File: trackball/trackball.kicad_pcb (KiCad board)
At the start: 2 copper layers, 15 x 27.4 mm, 7 parts, among them P8 CONN_7, U1 TLE4964-5M, U2 TLE4964-5M, U3 TLE4964-5M, U4 TLE4964-5M

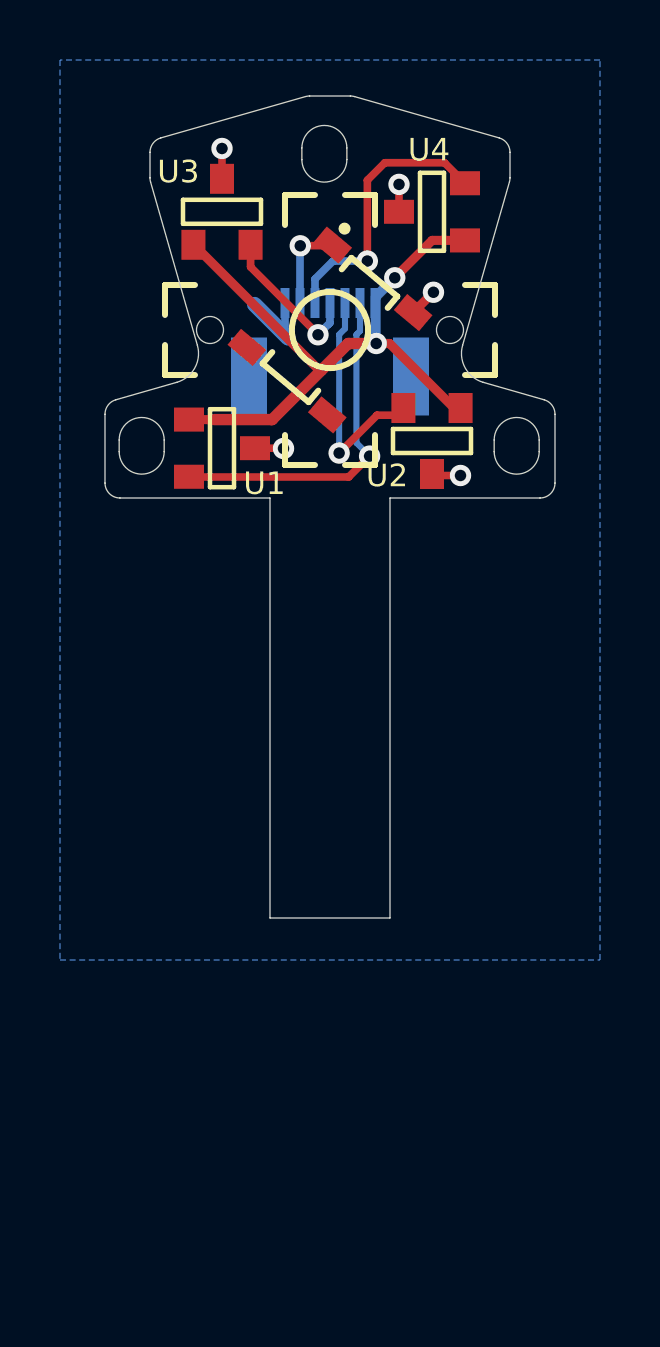
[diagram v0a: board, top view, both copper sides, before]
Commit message: Add most FPC tracks.
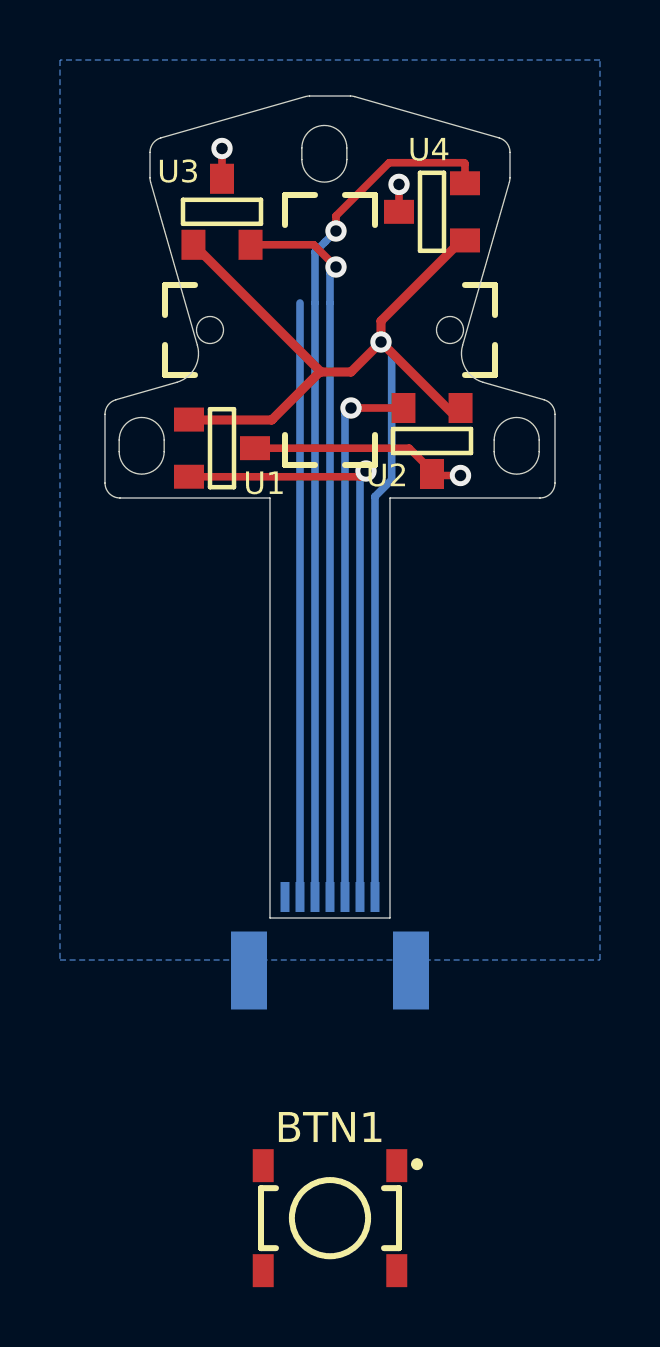
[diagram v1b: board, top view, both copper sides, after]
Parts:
- moved BTN1 29.6 mm to (200.0, 179.6), turned to 0 degrees
- moved P8 19.8 mm to (200.0, 172.9)
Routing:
- net /TB_RIGHT: track 9.58 -> 29.4 mm
- net /TB_UP: track 5.15 -> 24.5 mm
- net +3V3: track 22.5 -> 40.2 mm, vias 2 -> 1
- net /TB_BTN: track 4.14 -> 20.2 mm, vias 1 -> 0
- net /TB_DOWN: track 7.85 -> 18.5 mm
- net /TB_LEFT: track 11.5 -> 20.6 mm
- net GND: track 7.25 -> 9.03 mm, vias 5 -> 3

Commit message: Fix switch position and orientation.
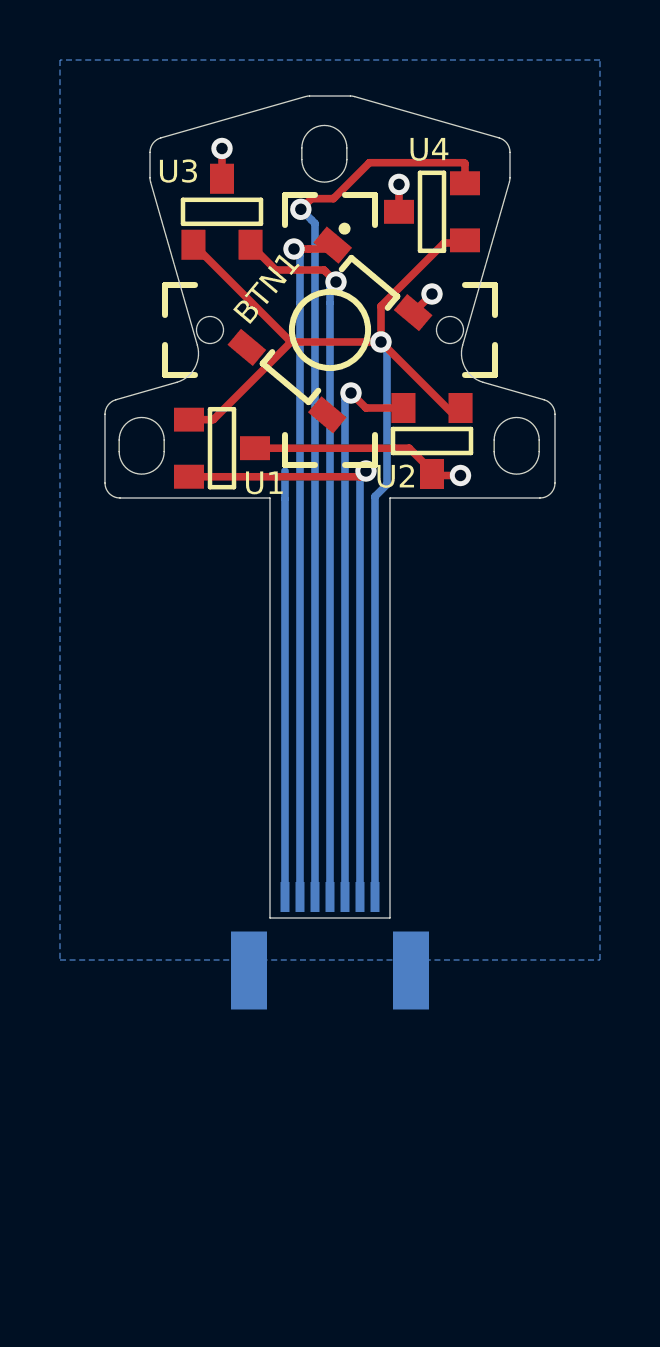
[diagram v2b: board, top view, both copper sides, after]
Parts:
- moved BTN1 29.6 mm to (200.0, 150.0), turned to 50 degrees
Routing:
- net GND: track 9.03 -> 24.1 mm, vias 3 -> 4
- net /TB_BTN: track 20.2 -> 23.1 mm, vias 0 -> 1
- net /TB_RIGHT: track 29.4 -> 30.6 mm
- net +3V3: track 40.2 -> 39.5 mm
- net /TB_DOWN: track 18.5 -> 19.2 mm
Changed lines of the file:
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@@
     (thickness 1.6)
     (drawings 46)
-    (tracks 57)
+    (tracks 68)
     (zones 0)
     (modules 7)
@@
     (tags SOT23)
     (attr smd)
-    (fp_text reference U2 (at 1.5 -1.16) (layer F.SilkS)
+    (fp_text reference U2 (at 1.2 -1.2) (layer F.SilkS)
       (effects (font (size 0.75 0.75) (thickness 0.15)))
     )
@@
   )
   (module UGL:TL3315NF250Q (layer F.Cu)
-    (at 200.000001 179.605001)
-    (fp_text reference BTN1 (at 0 -3) (layer F.SilkS)
-      (effects (font (size 1 1) (thickness 0.15)))
-    )
-    (fp_text value BTN (at 0 3.1) (layer F.Fab)
+    (at 200 150 50)
+    (fp_text reference BTN1 (at -0.277392 -2.508596 50) (layer F.SilkS)
+      (effects (font (size 0.75 0.75) (thickness 0.15)))
+    )
+    (fp_text value BTN (at 0 3.1 50) (layer F.Fab)
       (effects (font (size 1 1) (thickness 0.15)))
     )
@@
     (fp_line (start 2.3 1) (end 2.3 -1) (layer F.SilkS) (width 0.2))
     (fp_circle (center 2.9 -1.8) (end 3 -1.8) (layer F.SilkS) (width 0.2))
-    (pad 2 smd rect (at 2.225 1.75) (size 0.7 1.1) (layers F.Cu F.Paste F.Mask)
+    (pad 2 smd rect (at 2.225 1.75 50) (size 0.7 1.1) (layers F.Cu F.Paste F.Mask)
       (net 1 GND))
-    (pad 3 smd rect (at -2.225 1.75 180) (size 0.7 1.1) (layers F.Cu F.Paste F.Mask))
-    (pad 1 smd rect (at 2.225 -1.75) (size 0.7 1.1) (layers F.Cu F.Paste F.Mask)
+    (pad 3 smd rect (at -2.225 1.75 230) (size 0.7 1.1) (layers F.Cu F.Paste F.Mask))
+    (pad 1 smd rect (at 2.225 -1.75 50) (size 0.7 1.1) (layers F.Cu F.Paste F.Mask)
       (net 2 /TB_BTN))
-    (pad 4 smd rect (at -2.225 -1.75 180) (size 0.7 1.1) (layers F.Cu F.Paste F.Mask))
+    (pad 4 smd rect (at -2.225 -1.75 230) (size 0.7 1.1) (layers F.Cu F.Paste F.Mask))
   )
   (gr_line (start 202 155.6) (end 207 155.6) (angle 90) (layer Edge.Cuts) (width 0.01))
@@
   (segment (start 197.49982 153.94) (end 202.64 153.94) (width 0.254) (layer F.Cu) (net 1))
   (segment (start 202.64 153.94) (end 203.3 154.6) (width 0.254) (layer F.Cu) (net 1))
+  (via (at 203.4 148.8) (size 0.7112) (drill 0.381) (layers F.Cu B.Cu) (net 1))
+  (segment (start 202.77078 149.420429) (end 202.779571 149.420429) (width 0.254) (layer F.Cu) (net 1))
+  (segment (start 202.779571 149.420429) (end 203.4 148.8) (width 0.254) (layer F.Cu) (net 1))
+  (segment (start 198.5 168.9) (end 198.5 155.625942) (width 0.254) (layer B.Cu) (net 1))
+  (segment (start 198.5 155.625942) (end 198.5 154.7) (width 0.254) (layer B.Cu) (net 1))
   (segment (start 199 149.1) (end 199 169.26479) (width 0.254) (layer B.Cu) (net 2))
+  (via (at 198.8 147.3) (size 0.7112) (drill 0.381) (layers F.Cu B.Cu) (net 2))
+  (segment (start 199 149.1) (end 199 147.5) (width 0.254) (layer B.Cu) (net 2))
+  (segment (start 199 147.5) (end 198.8 147.3) (width 0.254) (layer B.Cu) (net 2))
+  (segment (start 198.8 147.3) (end 199.302894 147.3) (width 0.254) (layer F.Cu) (net 2))
+  (segment (start 199.302894 147.3) (end 199.9 147.3) (width 0.254) (layer F.Cu) (net 2))
   (segment (start 195.30018 154.8925) (end 195.30768 154.9) (width 0.254) (layer F.Cu) (net 3))
   (segment (start 201.0075 154.8925) (end 201.2 154.7) (width 0.254) (layer F.Cu) (net 3))
@@
   (segment (start 201.602894 150.5) (end 201.6 150.5) (width 0.3048) (layer F.Cu) (net 4))
   (via (at 201.7 150.4) (size 0.7112) (drill 0.381) (layers F.Cu B.Cu) (net 4))
-  (segment (start 201.7 150.4) (end 201.7 149.7) (width 0.3048) (layer F.Cu) (net 4))
-  (segment (start 201.7 149.7) (end 204.2 147.2) (width 0.3048) (layer F.Cu) (net 4))
-  (segment (start 198.071162 152.9875) (end 198.058662 153) (width 0.3048) (layer F.Cu) (net 4))
-  (segment (start 198.058662 153) (end 195.5 153) (width 0.3048) (layer F.Cu) (net 4))
-  (segment (start 198.071162 152.9875) (end 199.658662 151.4) (width 0.3048) (layer F.Cu) (net 4))
-  (segment (start 201.7 150.4) (end 200.7 151.4) (width 0.3048) (layer F.Cu) (net 4))
-  (segment (start 200.7 151.4) (end 199.7 151.4) (width 0.3048) (layer F.Cu) (net 4))
-  (segment (start 199.7 151.4) (end 195.6 147.3) (width 0.3048) (layer F.Cu) (net 4))
   (segment (start 201.75 150.45) (end 201.7 150.45) (width 0.3048) (layer F.Cu) (net 4))
   (segment (start 201.7 150.45) (end 201.7 150.4) (width 0.3048) (layer F.Cu) (net 4))
   (segment (start 204.3525 152.84018) (end 204.14018 152.84018) (width 0.3048) (layer F.Cu) (net 4))
-  (segment (start 204.14018 152.84018) (end 201.75 150.45) (width 0.3048) (layer F.Cu) (net 4))
-  (segment (start 202.055599 154.993888) (end 201.5 155.549487) (width 0.254) (layer B.Cu) (net 4))
-  (segment (start 202.055599 150.755599) (end 202.055599 154.993888) (width 0.254) (layer B.Cu) (net 4))
-  (segment (start 201.7 150.4) (end 202.055599 150.755599) (width 0.254) (layer B.Cu) (net 4))
+  (segment (start 195.30018 152.9875) (end 196.1125 152.9875) (width 0.254) (layer F.Cu) (net 4))
+  (segment (start 196.1125 152.9875) (end 198.7 150.4) (width 0.254) (layer F.Cu) (net 4))
+  (segment (start 201.7 150.4) (end 198.7 150.4) (width 0.254) (layer F.Cu) (net 4))
+  (segment (start 198.7 150.4) (end 195.6 147.3) (width 0.254) (layer F.Cu) (net 4))
+  (segment (start 201.7 149.206222) (end 203.806222 147.1) (width 0.254) (layer F.Cu) (net 4))
+  (segment (start 201.7 150.4) (end 201.7 149.206222) (width 0.254) (layer F.Cu) (net 4))
+  (segment (start 203.806222 147.1) (end 204.3 147.1) (width 0.254) (layer F.Cu) (net 4))
+  (segment (start 201.7 150.4) (end 204.2 152.9) (width 0.254) (layer F.Cu) (net 4))
   (segment (start 201.5 155.549487) (end 201.5 169.26479) (width 0.254) (layer B.Cu) (net 4))
-  (via (at 200.7 152.6) (size 0.7112) (drill 0.381) (layers F.Cu B.Cu) (net 5))
-  (segment (start 202.4475 152.60018) (end 200.70018 152.60018) (width 0.254) (layer F.Cu) (net 5))
-  (segment (start 200.70018 152.60018) (end 200.7 152.6) (width 0.254) (layer F.Cu) (net 5))
-  (segment (start 200.5 152.8) (end 200.5 169.26479) (width 0.254) (layer B.Cu) (net 5))
-  (segment (start 200.7 152.6) (end 200.5 152.8) (width 0.254) (layer B.Cu) (net 5))
+  (segment (start 201.9 155.149487) (end 201.5 155.549487) (width 0.254) (layer B.Cu) (net 4))
+  (segment (start 201.7 150.4) (end 201.9 150.6) (width 0.254) (layer B.Cu) (net 4))
+  (segment (start 201.9 150.6) (end 201.9 155.149487) (width 0.254) (layer B.Cu) (net 4))
+  (segment (start 202.4475 152.60018) (end 201.20018 152.60018) (width 0.254) (layer F.Cu) (net 5))
+  (via (at 200.7 152.1) (size 0.7112) (drill 0.381) (layers F.Cu B.Cu) (net 5))
+  (segment (start 201.20018 152.60018) (end 200.7 152.1) (width 0.254) (layer F.Cu) (net 5))
+  (segment (start 200.5 152.3) (end 200.7 152.1) (width 0.254) (layer B.Cu) (net 5))
+  (segment (start 200.5 169.26479) (end 200.5 152.3) (width 0.254) (layer B.Cu) (net 5))
   (segment (start 200 149.1) (end 200 169.26479) (width 0.254) (layer B.Cu) (net 6))
-  (via (at 200.2 147.9) (size 0.7112) (drill 0.381) (layers F.Cu B.Cu) (net 6))
-  (segment (start 200 149.1) (end 200 148.1) (width 0.254) (layer B.Cu) (net 6))
-  (segment (start 200 148.1) (end 200.1 148) (width 0.254) (layer B.Cu) (net 6))
-  (segment (start 197.3525 147.15982) (end 199.45982 147.15982) (width 0.254) (layer F.Cu) (net 6))
-  (segment (start 199.45982 147.15982) (end 200.2 147.9) (width 0.254) (layer F.Cu) (net 6))
+  (via (at 200.200006 148.4) (size 0.7112) (drill 0.381) (layers F.Cu B.Cu) (net 6))
+  (segment (start 200 149.1) (end 200 148.6) (width 0.254) (layer B.Cu) (net 6))
+  (segment (start 200 148.6) (end 200.2 148.4) (width 0.254) (layer B.Cu) (net 6))
+  (segment (start 199.844407 148.044401) (end 200.200006 148.4) (width 0.254) (layer F.Cu) (net 6))
+  (segment (start 197.3525 147.15982) (end 198.19268 148) (width 0.254) (layer F.Cu) (net 6))
+  (segment (start 199.800006 148) (end 199.844407 148.044401) (width 0.254) (layer F.Cu) (net 6))
+  (segment (start 198.19268 148) (end 199.800006 148) (width 0.254) (layer F.Cu) (net 6))
   (segment (start 204.615 145.2552) (end 204.3938 145.034) (width 0.3048) (layer F.Cu) (net 7))
-  (segment (start 199.5 149.1) (end 199.5 169.26479) (width 0.254) (layer B.Cu) (net 7))
-  (via (at 200.2 146.7) (size 0.7112) (drill 0.381) (layers F.Cu B.Cu) (net 7))
+  (segment (start 201.311921 144.4244) (end 200.115021 145.6213) (width 0.254) (layer F.Cu) (net 7))
+  (via (at 199.02853 145.976899) (size 0.7112) (drill 0.381) (layers F.Cu B.Cu) (net 7))
+  (segment (start 199.5 169.26479) (end 199.5 146.448369) (width 0.254) (layer B.Cu) (net 7))
   (segment (start 204.49982 144.45345) (end 204.47077 144.4244) (width 0.254) (layer F.Cu) (net 7))
+  (segment (start 199.5 146.448369) (end 199.384129 146.332498) (width 0.254) (layer B.Cu) (net 7))
+  (segment (start 199.384129 146.332498) (end 199.02853 145.976899) (width 0.254) (layer B.Cu) (net 7))
+  (segment (start 204.47077 144.4244) (end 201.311921 144.4244) (width 0.254) (layer F.Cu) (net 7))
   (segment (start 204.49982 145.1075) (end 204.49982 144.45345) (width 0.254) (layer F.Cu) (net 7))
-  (segment (start 199.5 147.4) (end 199.844401 147.055599) (width 0.254) (layer B.Cu) (net 7))
-  (segment (start 199.844401 147.055599) (end 200.2 146.7) (width 0.254) (layer B.Cu) (net 7))
-  (segment (start 199.5 149.1) (end 199.5 147.4) (width 0.254) (layer B.Cu) (net 7))
-  (segment (start 200.2 146.197106) (end 200.2 146.7) (width 0.254) (layer F.Cu) (net 7))
-  (segment (start 201.972706 144.4244) (end 200.2 146.197106) (width 0.254) (layer F.Cu) (net 7))
-  (segment (start 204.47077 144.4244) (end 201.972706 144.4244) (width 0.254) (layer F.Cu) (net 7))
+  (segment (start 200.115021 145.6213) (end 199.384129 145.6213) (width 0.254) (layer F.Cu) (net 7))
+  (segment (start 199.384129 145.6213) (end 199.02853 145.976899) (width 0.254) (layer F.Cu) (net 7))
   (zone (net 1) (net_name GND) (layer B.Cu) (hatch edge 0.508)
     (connect_pads (clearance 0.3048))

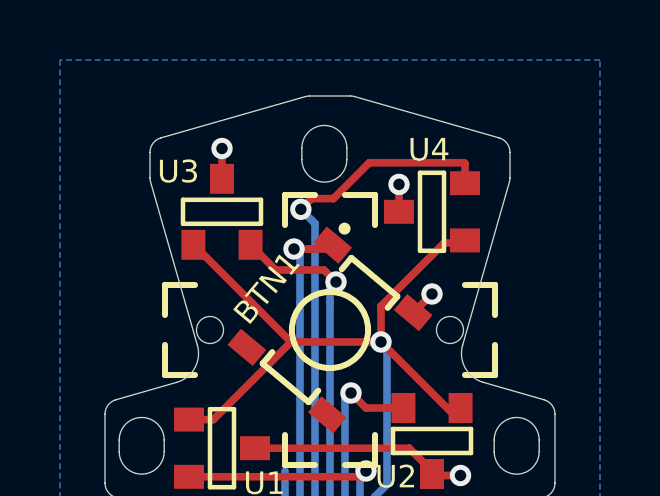
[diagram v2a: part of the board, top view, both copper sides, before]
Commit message: Slightly tidy up routing.
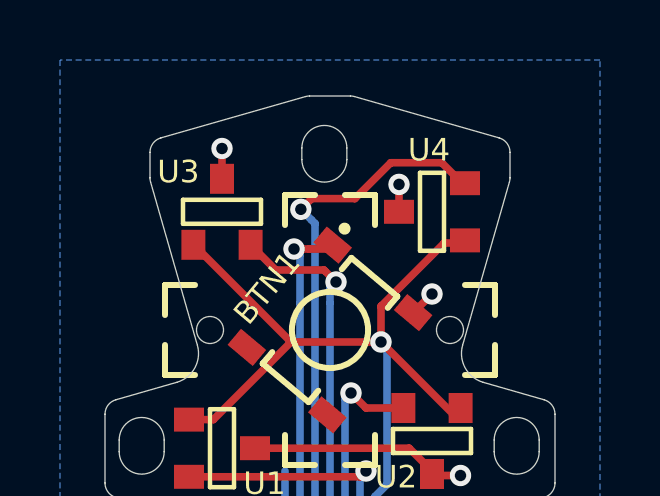
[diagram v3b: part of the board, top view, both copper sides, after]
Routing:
- net /TB_RIGHT: track 30.6 -> 29.7 mm
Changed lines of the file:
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@@
     (thickness 1.6)
     (drawings 46)
-    (tracks 68)
+    (tracks 67)
     (zones 0)
     (modules 7)
@@
   (segment (start 198.19268 148) (end 199.800006 148) (width 0.254) (layer F.Cu) (net 6))
   (segment (start 204.615 145.2552) (end 204.3938 145.034) (width 0.3048) (layer F.Cu) (net 7))
-  (segment (start 201.311921 144.4244) (end 200.115021 145.6213) (width 0.254) (layer F.Cu) (net 7))
   (via (at 199.02853 145.976899) (size 0.7112) (drill 0.381) (layers F.Cu B.Cu) (net 7))
   (segment (start 199.5 169.26479) (end 199.5 146.448369) (width 0.254) (layer B.Cu) (net 7))
-  (segment (start 204.49982 144.45345) (end 204.47077 144.4244) (width 0.254) (layer F.Cu) (net 7))
   (segment (start 199.5 146.448369) (end 199.384129 146.332498) (width 0.254) (layer B.Cu) (net 7))
   (segment (start 199.384129 146.332498) (end 199.02853 145.976899) (width 0.254) (layer B.Cu) (net 7))
-  (segment (start 204.47077 144.4244) (end 201.311921 144.4244) (width 0.254) (layer F.Cu) (net 7))
-  (segment (start 204.49982 145.1075) (end 204.49982 144.45345) (width 0.254) (layer F.Cu) (net 7))
-  (segment (start 200.115021 145.6213) (end 199.384129 145.6213) (width 0.254) (layer F.Cu) (net 7))
   (segment (start 199.384129 145.6213) (end 199.02853 145.976899) (width 0.254) (layer F.Cu) (net 7))
+  (segment (start 200.8287 145.6213) (end 199.384129 145.6213) (width 0.254) (layer F.Cu) (net 7))
+  (segment (start 202.0256 144.4244) (end 200.8287 145.6213) (width 0.254) (layer F.Cu) (net 7))
+  (segment (start 202.0256 144.4244) (end 203.7244 144.4244) (width 0.254) (layer F.Cu) (net 7))
+  (segment (start 203.7244 144.4244) (end 204.1 144.8) (width 0.254) (layer F.Cu) (net 7))
   (zone (net 1) (net_name GND) (layer B.Cu) (hatch edge 0.508)
     (connect_pads (clearance 0.3048))
